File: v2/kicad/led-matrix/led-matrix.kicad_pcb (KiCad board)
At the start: 2 copper layers, 38 x 38 mm, 6 parts, among them J1 Conn_02x03_Input, J2 Conn_02x03_Output, U1 MAX7219

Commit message: Routing attempt 1
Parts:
- J1: footprint led-matrix:PinSocket_2x03_P2.54mm_Horizontal -> Connector_PinSocket_2.54mm:PinSocket_2x03_P2.54mm_Horizontal
- moved R1 7.15 mm to (121.7, 128.3), turned to 90 degrees
- moved C1 5.69 mm to (116.3, 128.6), turned to 0 degrees
- moved U1 4.55 mm to (121.5, 119.5)
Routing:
- net load: track 0.00 -> 47.7 mm, vias 0 -> 1
- net D_fwd: track 0.00 -> 47.4 mm
- net Vcc: track 5.51 -> 44.1 mm, vias 0 -> 1
- net clk: track 0.00 -> 34.8 mm, vias 0 -> 1
- net Dout: track 0.00 -> 32.7 mm, vias 0 -> 1
- net row2: track 0.00 -> 28.8 mm
- net row5: track 0.00 -> 28.0 mm
- net column7: track 0.00 -> 26.9 mm
- net row4: track 0.00 -> 24.1 mm
- net column1: track 0.00 -> 23.7 mm
- net row7: track 0.00 -> 23.5 mm, vias 0 -> 1
- net column2: track 0.00 -> 21.8 mm, vias 0 -> 1
- net column5: track 0.00 -> 21.4 mm
- net column4: track 0.00 -> 21.2 mm, vias 0 -> 1
- net column6: track 0.00 -> 20.7 mm, vias 0 -> 1
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- added copper zone on B.Cu, net GND
- added copper zone on F.Cu, net GND

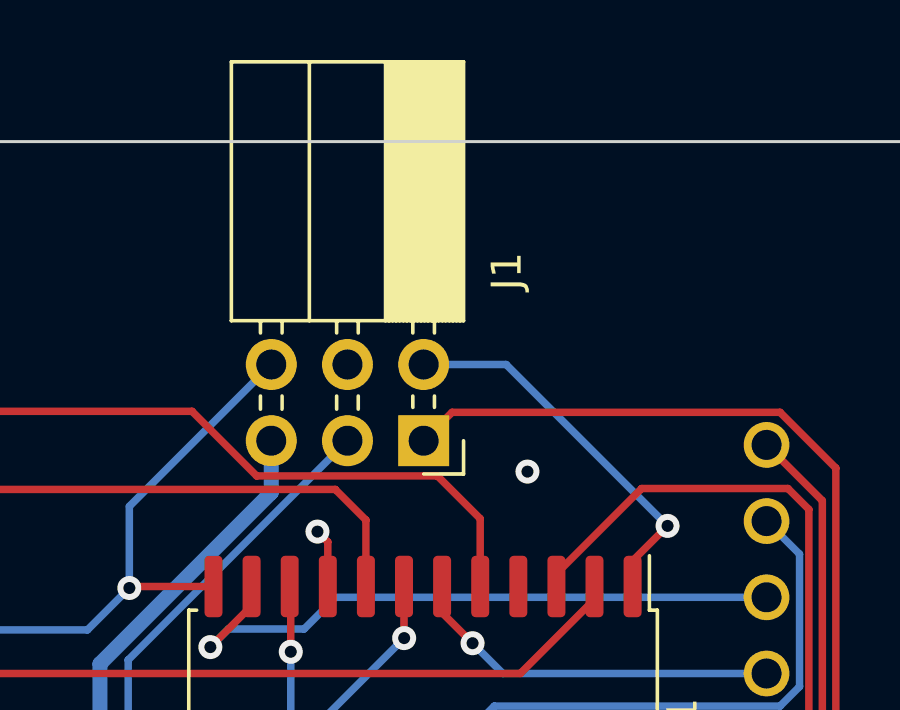
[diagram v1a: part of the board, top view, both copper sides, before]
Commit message: fix female header
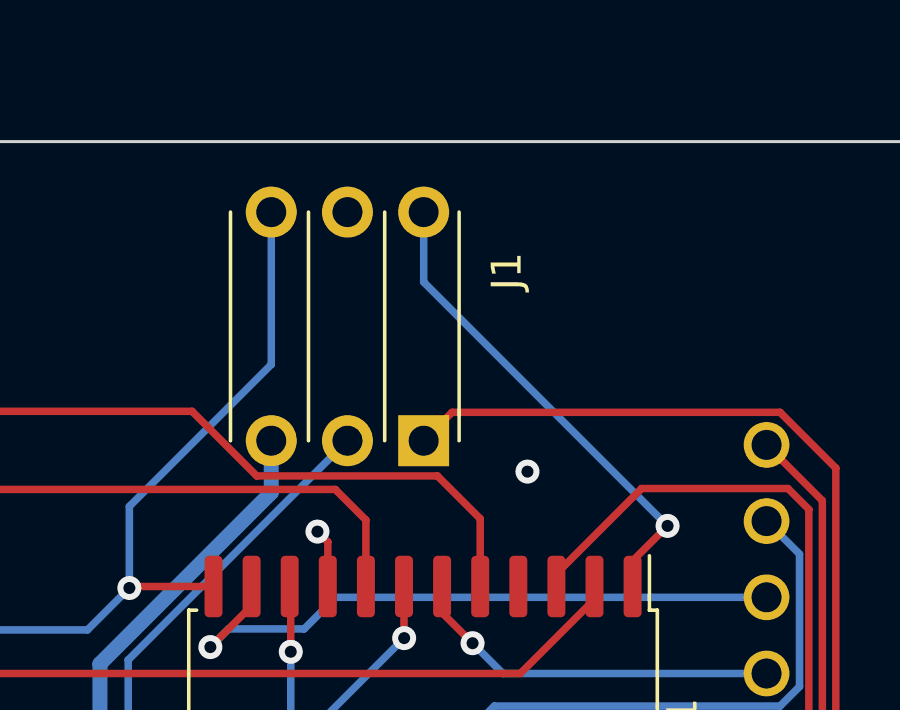
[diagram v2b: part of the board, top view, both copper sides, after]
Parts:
- J1: footprint Connector_PinSocket_2.54mm:PinSocket_2x03_P2.54mm_Horizontal -> led-matrix:PinSocket_2x03_P2.54mm_Horizontal
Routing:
- net load: track 47.7 -> 52.8 mm
- net Din: track 12.9 -> 16.3 mm
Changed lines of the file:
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@@
   (net 23 "Dout")
   (net 24 "Net-(R1-Pad2)")
-  (footprint "Connector_PinSocket_2.54mm:PinSocket_2x03_P2.54mm_Horizontal" (layer "F.Cu")
+  (footprint "led-matrix:PinSocket_2x03_P2.54mm_Horizontal" (layer "F.Cu")
     (at 121.54 109.97 -90)
     (descr "Through hole angled socket strip, 2x03, 2.54mm pitch, 8.51mm socket length, double cols (from Kicad 4.0.7), script generated")
@@
       (effects (font (size 1 1) (thickness 0.15)))
     )
-    (fp_line (start -1.49 -0.36) (end -1.11 -0.36) (layer "F.SilkS") (width 0.12))
-    (fp_line (start -4 -1.33) (end -4 6.41) (layer "F.SilkS") (width 0.12))
-    (fp_line (start -12.63 -0.855715) (end -4 -0.855715) (layer "F.SilkS") (width 0.12))
-    (fp_line (start -12.63 1.033805) (end -4 1.033805) (layer "F.SilkS") (width 0.12))
-    (fp_line (start -12.63 3.81) (end -4 3.81) (layer "F.SilkS") (width 0.12))
-    (fp_line (start -12.63 -1.21) (end -4 -1.21) (layer "F.SilkS") (width 0.12))
-    (fp_line (start 1.11 -1.33) (end 1.11 0) (layer "F.SilkS") (width 0.12))
-    (fp_line (start -12.63 0.089045) (end -4 0.089045) (layer "F.SilkS") (width 0.12))
-    (fp_line (start -4 -0.36) (end -3.59 -0.36) (layer "F.SilkS") (width 0.12))
-    (fp_line (start 0 -1.33) (end 1.11 -1.33) (layer "F.SilkS") (width 0.12))
-    (fp_line (start -12.63 0.20714) (end -4 0.20714) (layer "F.SilkS") (width 0.12))
-    (fp_line (start -12.63 1.1519) (end -4 1.1519) (layer "F.SilkS") (width 0.12))
-    (fp_line (start -12.63 0.67952) (end -4 0.67952) (layer "F.SilkS") (width 0.12))
-    (fp_line (start -12.63 0.91571) (end -4 0.91571) (layer "F.SilkS") (width 0.12))
-    (fp_line (start -12.63 -0.619525) (end -4 -0.619525) (layer "F.SilkS") (width 0.12))
-    (fp_line (start -1.49 0.36) (end -1.11 0.36) (layer "F.SilkS") (width 0.12))
-    (fp_line (start -1.49 2.18) (end -1.05 2.18) (layer "F.SilkS") (width 0.12))
-    (fp_line (start -12.63 -1.33) (end -4 -1.33) (layer "F.SilkS") (width 0.12))
-    (fp_line (start -1.49 4.72) (end -1.05 4.72) (layer "F.SilkS") (width 0.12))
-    (fp_line (start -12.63 -0.147145) (end -4 -0.147145) (layer "F.SilkS") (width 0.12))
-    (fp_line (start -4 0.36) (end -3.59 0.36) (layer "F.SilkS") (width 0.12))
-    (fp_line (start -12.63 -0.26524) (end -4 -0.26524) (layer "F.SilkS") (width 0.12))
-    (fp_line (start -1.49 2.9) (end -1.05 2.9) (layer "F.SilkS") (width 0.12))
-    (fp_line (start -12.63 -1.33) (end -12.63 6.41) (layer "F.SilkS") (width 0.12))
-    (fp_line (start -4 4.72) (end -3.59 4.72) (layer "F.SilkS") (width 0.12))
-    (fp_line (start -12.63 -0.73762) (end -4 -0.73762) (layer "F.SilkS") (width 0.12))
-    (fp_line (start -12.63 0.561425) (end -4 0.561425) (layer "F.SilkS") (width 0.12))
-    (fp_line (start -12.63 -0.50143) (end -4 -0.50143) (layer "F.SilkS") (width 0.12))
-    (fp_line (start -1.49 5.44) (end -1.05 5.44) (layer "F.SilkS") (width 0.12))
-    (fp_line (start -12.63 0.44333) (end -4 0.44333) (layer "F.SilkS") (width 0.12))
-    (fp_line (start -12.63 1.27) (end -4 1.27) (layer "F.SilkS") (width 0.12))
-    (fp_line (start -12.63 -0.97381) (end -4 -0.97381) (layer "F.SilkS") (width 0.12))
-    (fp_line (start -12.63 6.41) (end -4 6.41) (layer "F.SilkS") (width 0.12))
-    (fp_line (start -4 5.44) (end -3.59 5.44) (layer "F.SilkS") (width 0.12))
-    (fp_line (start -12.63 -0.02905) (end -4 -0.02905) (layer "F.SilkS") (width 0.12))
-    (fp_line (start -12.63 0.325235) (end -4 0.325235) (layer "F.SilkS") (width 0.12))
-    (fp_line (start -4 2.9) (end -3.59 2.9) (layer "F.SilkS") (width 0.12))
-    (fp_line (start -12.63 0.797615) (end -4 0.797615) (layer "F.SilkS") (width 0.12))
-    (fp_line (start -12.63 -0.383335) (end -4 -0.383335) (layer "F.SilkS") (width 0.12))
-    (fp_line (start -4 2.18) (end -3.59 2.18) (layer "F.SilkS") (width 0.12))
-    (fp_line (start -12.63 -1.091905) (end -4 -1.091905) (layer "F.SilkS") (width 0.12))
-    (fp_line (start -13.05 6.85) (end 1.8 6.85) (layer "F.CrtYd") (width 0.05))
-    (fp_line (start -13.05 -1.8) (end -13.05 6.85) (layer "F.CrtYd") (width 0.05))
-    (fp_line (start 1.8 6.85) (end 1.8 -1.8) (layer "F.CrtYd") (width 0.05))
-    (fp_line (start 1.8 -1.8) (end -13.05 -1.8) (layer "F.CrtYd") (width 0.05))
+    (fp_line (start -7.62 3.83905) (end 0 3.83905) (layer "F.SilkS") (width 0.12))
+    (fp_line (start -7.62 6.43905) (end 0 6.43905) (layer "F.SilkS") (width 0.12))
+    (fp_line (start -7.62 1.29905) (end 0 1.29905) (layer "F.SilkS") (width 0.12))
+    (fp_line (start -7.62 -1.18095) (end 0 -1.18095) (layer "F.SilkS") (width 0.12))
+    (fp_line (start 0 -1.8) (end -7.62 -1.8) (layer "F.CrtYd") (width 0.05))
+    (fp_line (start 0 6.85) (end 0 -1.8) (layer "F.CrtYd") (width 0.05))
+    (fp_line (start -7.62 6.85) (end 0 6.85) (layer "F.CrtYd") (width 0.05))
+    (fp_line (start -7.62 -1.8) (end -7.62 6.85) (layer "F.CrtYd") (width 0.05))
+    (fp_line (start -7.62 -1.27) (end -0.08 -1.27) (layer "F.Fab") (width 0.1))
+    (fp_line (start 0 5.38) (end 0 4.78) (layer "F.Fab") (width 0.1))
+    (fp_line (start 0.89 -0.3) (end 0.89 6.35) (layer "F.Fab") (width 0.1))
+    (fp_line (start -2.54 4.78) (end -6.6 4.78) (layer "F.Fab") (width 0.1))
+    (fp_line (start -2.54 -0.3) (end -6.6 -0.3) (layer "F.Fab") (width 0.1))
+    (fp_line (start 0.89 6.35) (end -7.62 6.35) (layer "F.Fab") (width 0.1))
+    (fp_line (start -7.62 6.35) (end -7.62 -1.27) (layer "F.Fab") (width 0.1))
+    (fp_line (start -2.54 2.24) (end -6.6 2.24) (layer "F.Fab") (width 0.1))
+    (fp_line (start 0 2.84) (end 0 2.24) (layer "F.Fab") (width 0.1))
+    (fp_line (start -6.6 5.38) (end -2.54 5.38) (layer "F.Fab") (width 0.1))
+    (fp_line (start -0.08 -1.27) (end 0.89 -0.3) (layer "F.Fab") (width 0.1))
     (fp_line (start 0 0.3) (end 0 -0.3) (layer "F.Fab") (width 0.1))
-    (fp_line (start -4.06 0.3) (end 0 0.3) (layer "F.Fab") (width 0.1))
-    (fp_line (start -4.06 -0.3) (end -4.06 6.35) (layer "F.Fab") (width 0.1))
-    (fp_line (start 0 5.38) (end 0 4.78) (layer "F.Fab") (width 0.1))
-    (fp_line (start 0 -0.3) (end -4.06 -0.3) (layer "F.Fab") (width 0.1))
-    (fp_line (start 0 2.24) (end -4.06 2.24) (layer "F.Fab") (width 0.1))
-    (fp_line (start -4.06 5.38) (end 0 5.38) (layer "F.Fab") (width 0.1))
-    (fp_line (start -4.06 2.84) (end 0 2.84) (layer "F.Fab") (width 0.1))
-    (fp_line (start -12.57 -1.27) (end -5.03 -1.27) (layer "F.Fab") (width 0.1))
-    (fp_line (start -5.03 -1.27) (end -4.06 -0.3) (layer "F.Fab") (width 0.1))
-    (fp_line (start 0 4.78) (end -4.06 4.78) (layer "F.Fab") (width 0.1))
-    (fp_line (start -12.57 6.35) (end -12.57 -1.27) (layer "F.Fab") (width 0.1))
-    (fp_line (start -4.06 6.35) (end -12.57 6.35) (layer "F.Fab") (width 0.1))
-    (fp_line (start 0 2.84) (end 0 2.24) (layer "F.Fab") (width 0.1))
+    (fp_line (start -6.6 0.3) (end -2.54 0.3) (layer "F.Fab") (width 0.1))
+    (fp_line (start -6.6 2.84) (end -2.54 2.84) (layer "F.Fab") (width 0.1))
     (pad "1" thru_hole rect (at 0 0 270) (size 1.7 1.7) (drill 1) (layers *.Cu *.Mask)
       (net 19 "D_fwd") (pinfunction "D_fwd") (pintype "input"))
-    (pad "2" thru_hole oval (at -2.54 0 270) (size 1.7 1.7) (drill 1) (layers *.Cu *.Mask)
+    (pad "2" thru_hole oval (at -7.62 0 270) (size 1.7 1.7) (drill 1) (layers *.Cu *.Mask)
       (net 20 "Din") (pinfunction "Din") (pintype "output"))
     (pad "3" thru_hole oval (at 0 2.54 270) (size 1.7 1.7) (drill 1) (layers *.Cu *.Mask)
       (net 21 "clk") (pinfunction "Clk_in") (pintype "output"))
-    (pad "4" thru_hole oval (at -2.54 2.54 270) (size 1.7 1.7) (drill 1) (layers *.Cu *.Mask)
+    (pad "4" thru_hole oval (at -7.62 2.54 270) (size 1.7 1.7) (drill 1) (layers *.Cu *.Mask)
       (net 1 "GND") (pinfunction "Gnd") (pintype "power_out"))
     (pad "5" thru_hole oval (at 0 5.08 270) (size 1.7 1.7) (drill 1) (layers *.Cu *.Mask)
       (net 2 "Vcc") (pinfunction "VCC") (pintype "power_in"))
-    (pad "6" thru_hole oval (at -2.54 5.08 270) (size 1.7 1.7) (drill 1) (layers *.Cu *.Mask)
+    (pad "6" thru_hole oval (at -7.62 5.08 270) (size 1.7 1.7) (drill 1) (layers *.Cu *.Mask)
       (net 22 "load") (pinfunction "load_in") (pintype "output"))
     (model "${KICAD6_3DMODEL_DIR}/Connector_PinSocket_2.54mm.3dshapes/PinSocket_2x03_P2.54mm_Horizontal.wrl"
@@
   (segment (start 128.505 114.83) (end 128.505 113.975) (width 0.25) (layer "F.Cu") (net 20))
   (via (at 129.67 112.81) (size 0.8) (drill 0.4) (layers "F.Cu" "B.Cu") (net 20))
-  (segment (start 124.29 107.43) (end 121.54 107.43) (width 0.25) (layer "B.Cu") (net 20))
-  (segment (start 129.67 112.81) (end 124.29 107.43) (width 0.25) (layer "B.Cu") (net 20))
+  (segment (start 121.54 104.68) (end 121.54 102.35) (width 0.25) (layer "B.Cu") (net 20))
+  (segment (start 129.67 112.81) (end 121.54 104.68) (width 0.25) (layer "B.Cu") (net 20))
   (segment (start 113.77048 132.08149) (end 113.77048 124.89452) (width 0.25) (layer "F.Cu") (net 21))
   (segment (start 119 133.11) (end 117.82 134.29) (width 0.25) (layer "F.Cu") (net 21))
@@
   (segment (start 116.46 135.65) (end 111.25344 135.65) (width 0.25) (layer "B.Cu") (net 22))
   (segment (start 104.853489 116.276511) (end 110.333489 116.276511) (width 0.25) (layer "B.Cu") (net 22))
+  (segment (start 116.46 107.43) (end 116.46 102.35) (width 0.25) (layer "B.Cu") (net 22))
   (segment (start 111.73 112.16) (end 116.46 107.43) (width 0.25) (layer "B.Cu") (net 22))
   (segment (start 110.333489 116.276511) (end 111.73 114.88) (width 0.25) (layer "B.Cu") (net 22))

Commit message: Fix DRC
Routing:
- net column6: track 20.7 -> 19.9 mm
- net GND: vias 3 -> 4
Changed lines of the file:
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@@
   (via (at 118 113) (size 0.8) (drill 0.4) (layers "F.Cu" "B.Cu") (net 1))
   (via (at 127 131) (size 0.8) (drill 0.4) (layers "F.Cu" "B.Cu") (free) (net 1))
+  (via (at 116.25 130.5) (size 0.8) (drill 0.4) (layers "F.Cu" "B.Cu") (free) (net 1))
   (segment (start 122.75 121.75) (end 122.010489 121.010489) (width 0.5) (layer "F.Cu") (net 2))
   (segment (start 122.99452 128.54548) (end 122.99452 125.99452) (width 0.5) (layer "F.Cu") (net 2))
@@
   (segment (start 120.89 116.55) (end 112.09 125.35) (width 0.25) (layer "B.Cu") (net 12))
   (segment (start 112.09 125.35) (end 105.03 125.35) (width 0.25) (layer "B.Cu") (net 12))
-  (segment (start 117.075 114.83) (end 117.075 115.695) (width 0.25) (layer "F.Cu") (net 13))
-  (segment (start 117.11 114.865) (end 117.075 114.83) (width 0.25) (layer "F.Cu") (net 13))
-  (segment (start 117.11 117.0055) (end 117.11 114.865) (width 0.25) (layer "F.Cu") (net 13))
+  (segment (start 117.075 114.83) (end 117.075 116.9705) (width 0.25) (layer "F.Cu") (net 13))
+  (segment (start 117.075 116.9705) (end 117.11 117.0055) (width 0.25) (layer "F.Cu") (net 13))
   (via (at 117.11 117.0055) (size 0.8) (drill 0.4) (layers "F.Cu" "B.Cu") (net 13))
   (segment (start 106.65 124.43) (end 105.03 122.81) (width 0.25) (layer "B.Cu") (net 13))
